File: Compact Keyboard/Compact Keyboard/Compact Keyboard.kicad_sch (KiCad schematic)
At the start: 3 parts, among them SW1 SW_Push

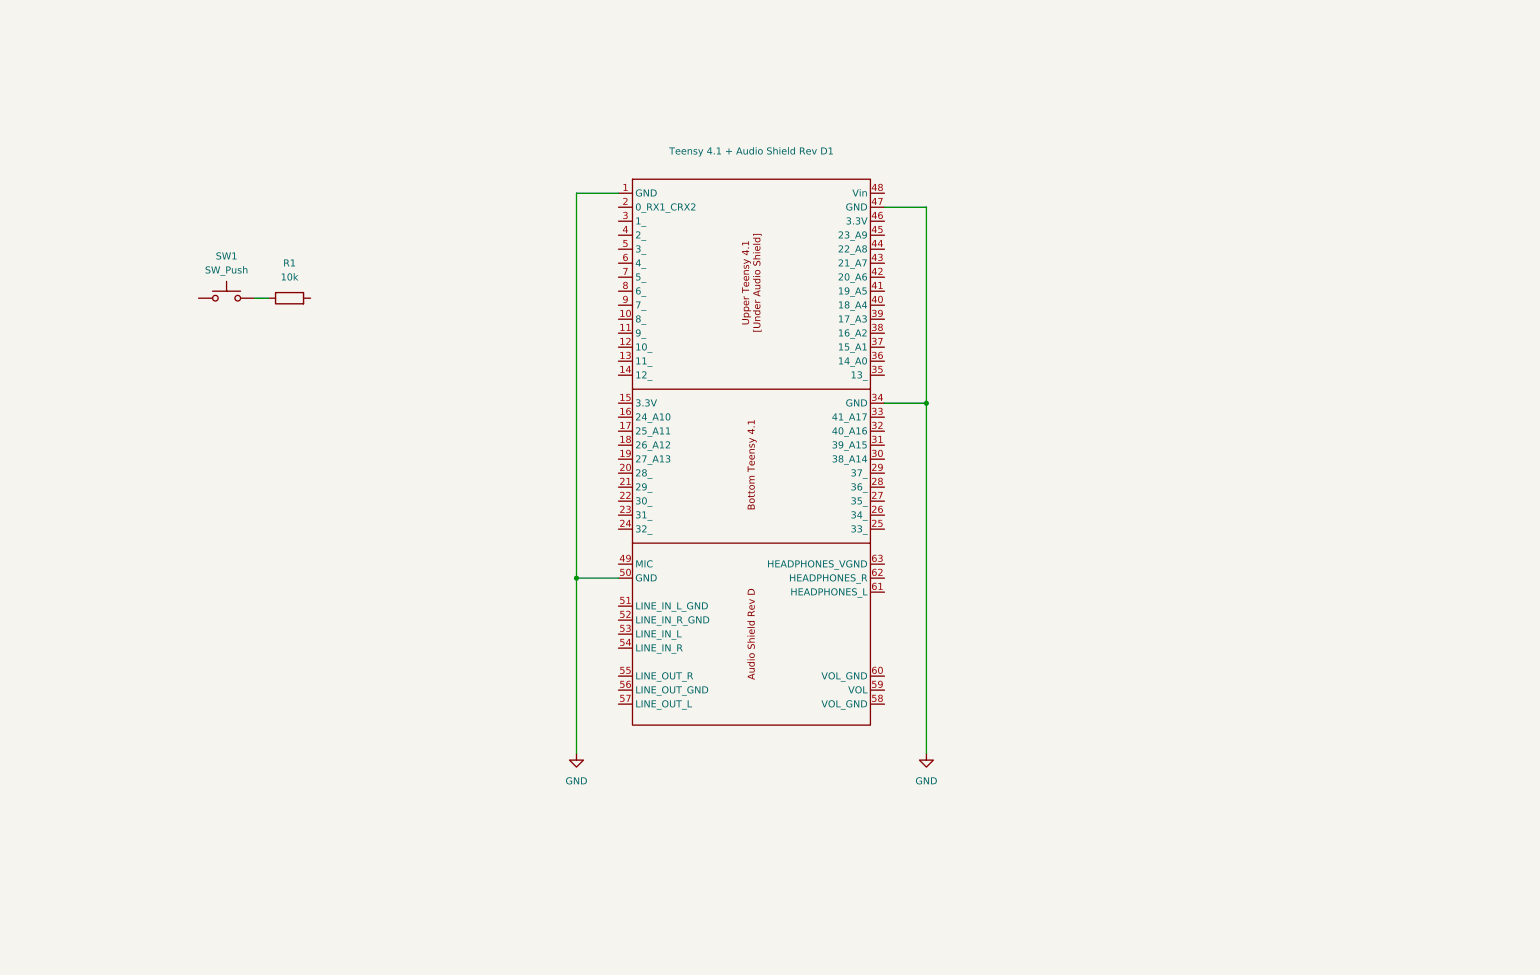
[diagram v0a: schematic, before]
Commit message: Smaller MUX, Main Board design
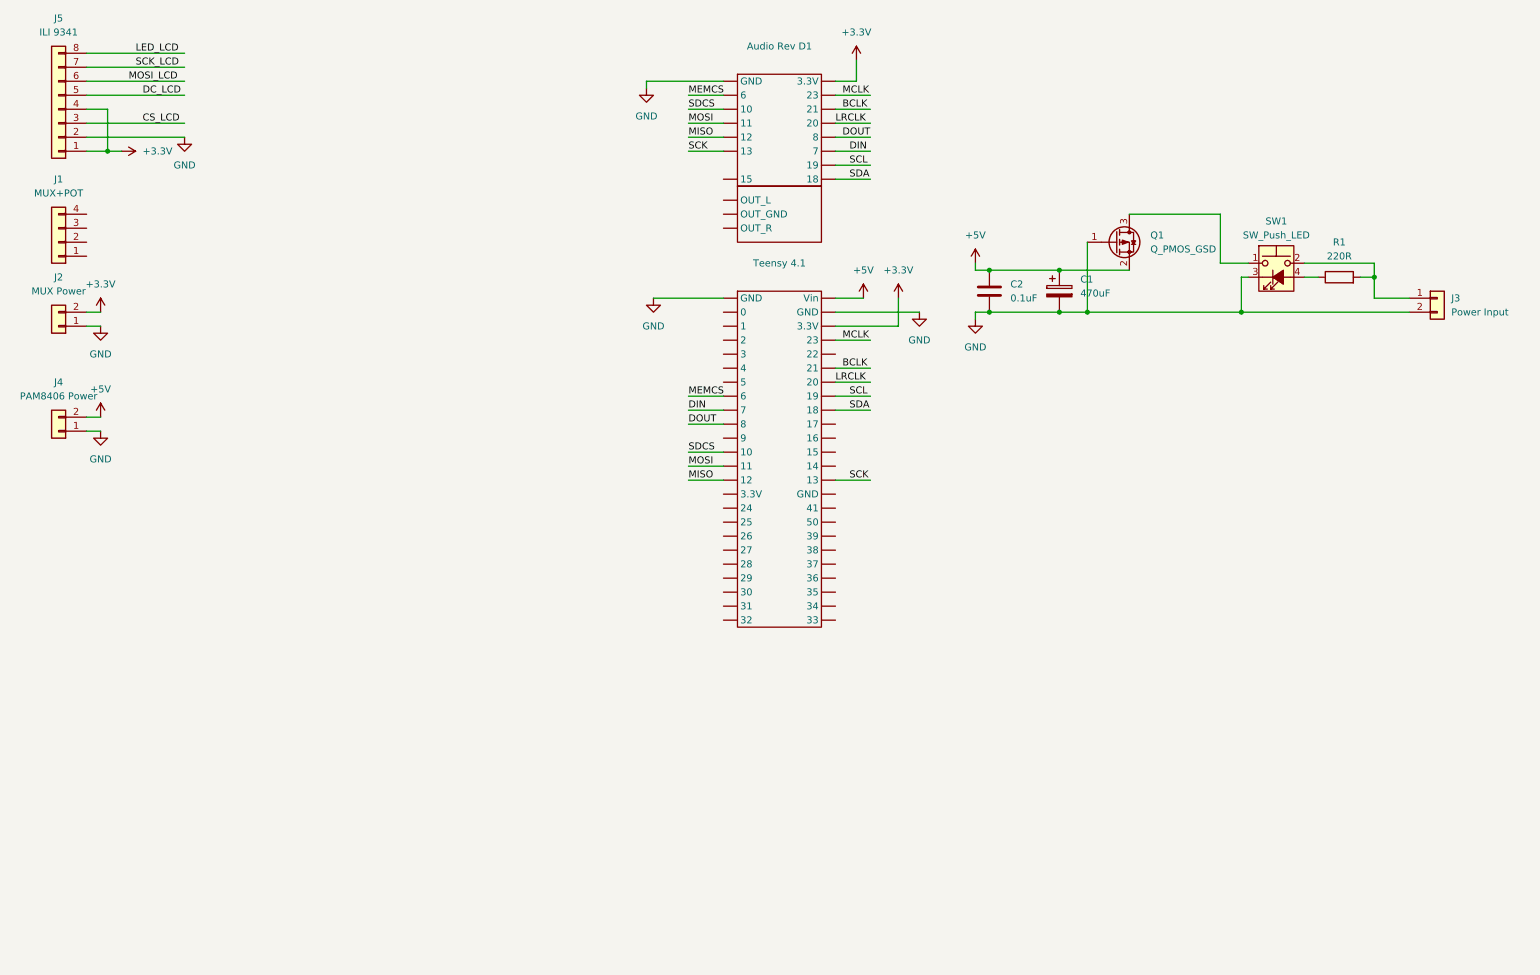
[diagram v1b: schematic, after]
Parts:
- removed SW1: SW_Push, symbol Switch:SW_Push
- removed Teensy 4.1 + Audio Shield Rev D1: ~, symbol Teensy:Teensy 4.1 + Audio Shield Rev D
- added Audio Rev D1: ~, symbol Teensy:Audio_Shield_Rev_D
- added C1: 470uF, symbol Device:C_Polarized
- added C2: 0.1uF, symbol Device:C
- added J1: MUX+POT, symbol Connector_Generic:Conn_01x04
- added J2: MUX Power, symbol Connector_Generic:Conn_01x02
- added J3: Power Input, symbol Connector_Generic:Conn_01x02
- added J4: PAM8406 Power, symbol Connector_Generic:Conn_01x02
- added J5: ILI 9341, symbol Connector_Generic:Conn_01x08
- added Q1: Q_PMOS_GSD, symbol Transistor_FET:Q_PMOS_GSD
- added SW1: SW_Push_LED, symbol Switch:SW_Push_LED
- added Teensy 4.1: ~, symbol Teensy:Teensy_4.1
- R1: value 10k -> 220R
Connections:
- net GND: now also Audio Rev D1. (18), C1.2, C2.2, J2.1 (Pin_1), J3.2 (Pin_2), J4.1 (Pin_1), J5.2 (Pin_2), Q1.1 (G), SW1.3 (K), Teensy 4.1. (33)
- net at R1.1: now also SW1.4 (A)
- net at R1.2: now also J3.1 (Pin_1), SW1.2
- new net: Q1.3 (D), SW1.1
- new net +3.3V: Audio Rev D1. (18), J2.2 (Pin_2), J5.1 (Pin_1), J5.4 (Pin_4), Teensy 4.1. (33)
- new net +5V: C1.1, C2.1, J4.2 (Pin_2), Q1.2 (S), Teensy 4.1. (33)
- new net BCLK: Audio Rev D1. (18), Teensy 4.1. (33)
- new net CS_LCD: J5.3 (Pin_3)
- new net DC_LCD: J5.5 (Pin_5)
- new net DIN: Audio Rev D1. (18), Teensy 4.1. (33)
- new net DOUT: Audio Rev D1. (18), Teensy 4.1. (33)
- new net LED_LCD: J5.8 (Pin_8)
- new net LRCLK: Audio Rev D1. (18), Teensy 4.1. (33)
- new net MCLK: Audio Rev D1. (18), Teensy 4.1. (33)
- new net MEMCS: Audio Rev D1. (18), Teensy 4.1. (33)
- new net MISO: Audio Rev D1. (18), Teensy 4.1. (33)
- new net MOSI: Audio Rev D1. (18), Teensy 4.1. (33)
- new net MOSI_LCD: J5.6 (Pin_6)
- new net SCK: Audio Rev D1. (18), Teensy 4.1. (33)
- new net SCK_LCD: J5.7 (Pin_7)
- new net SCL: Audio Rev D1. (18), Teensy 4.1. (33)
- new net SDA: Audio Rev D1. (18), Teensy 4.1. (33)
- new net SDCS: Audio Rev D1. (18), Teensy 4.1. (33)

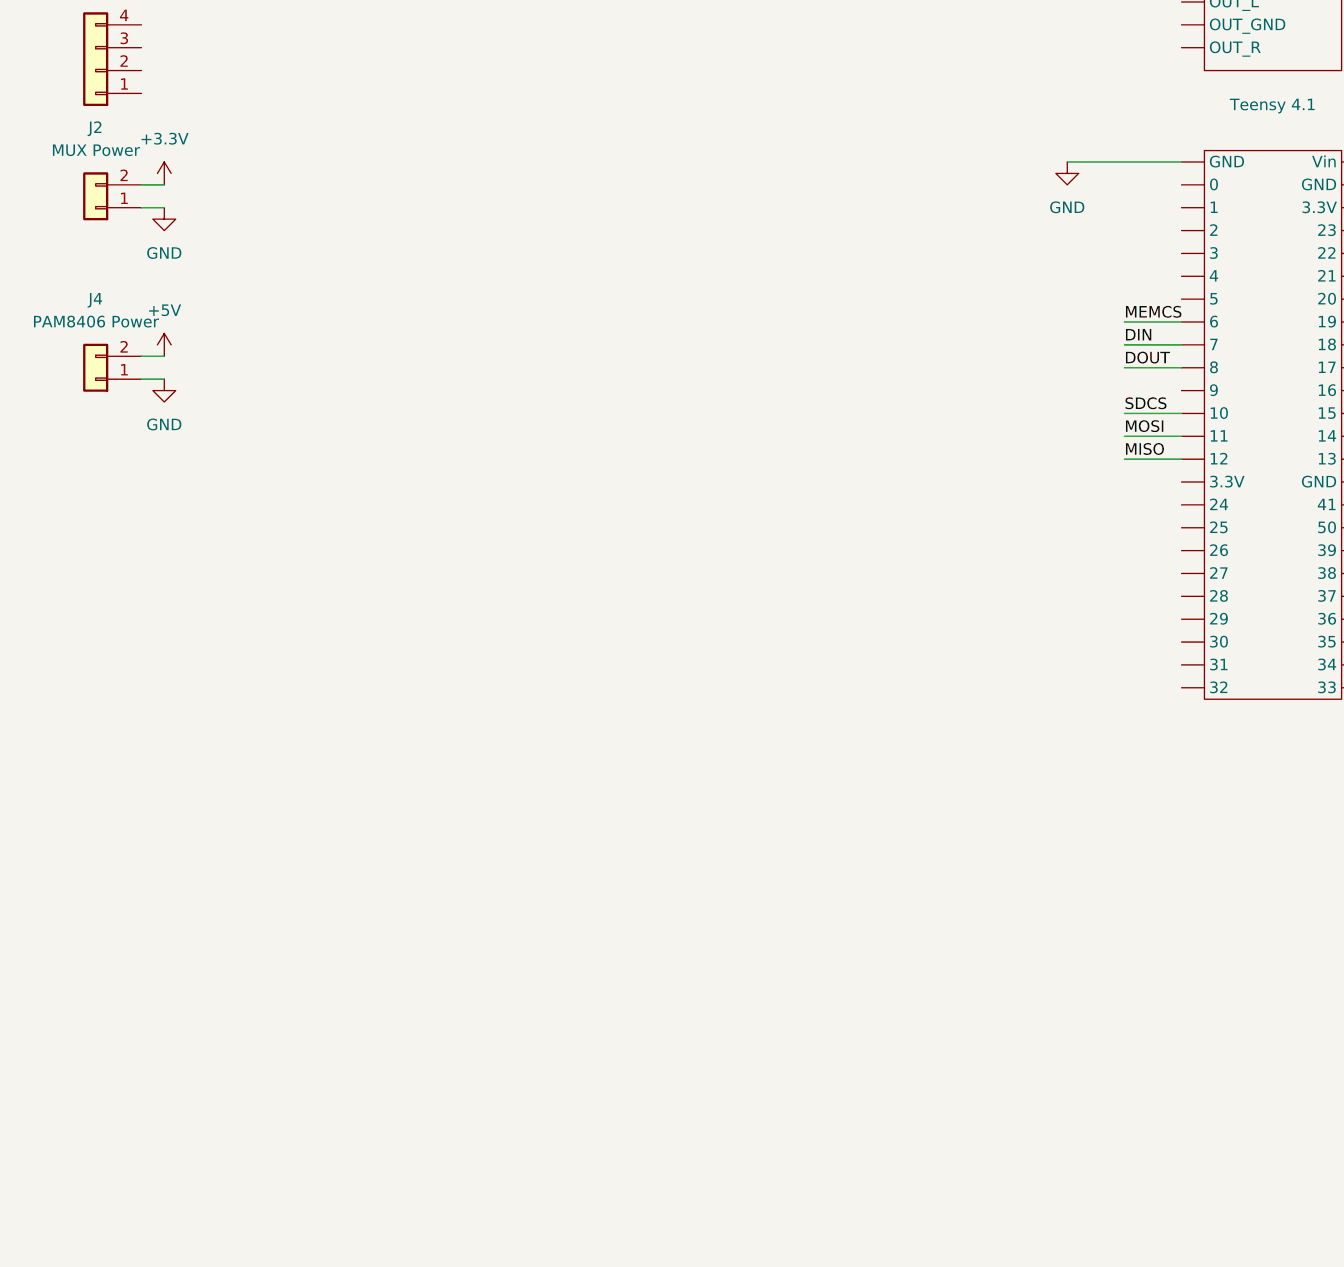
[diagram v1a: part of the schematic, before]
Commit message: More Inputs for Teensy
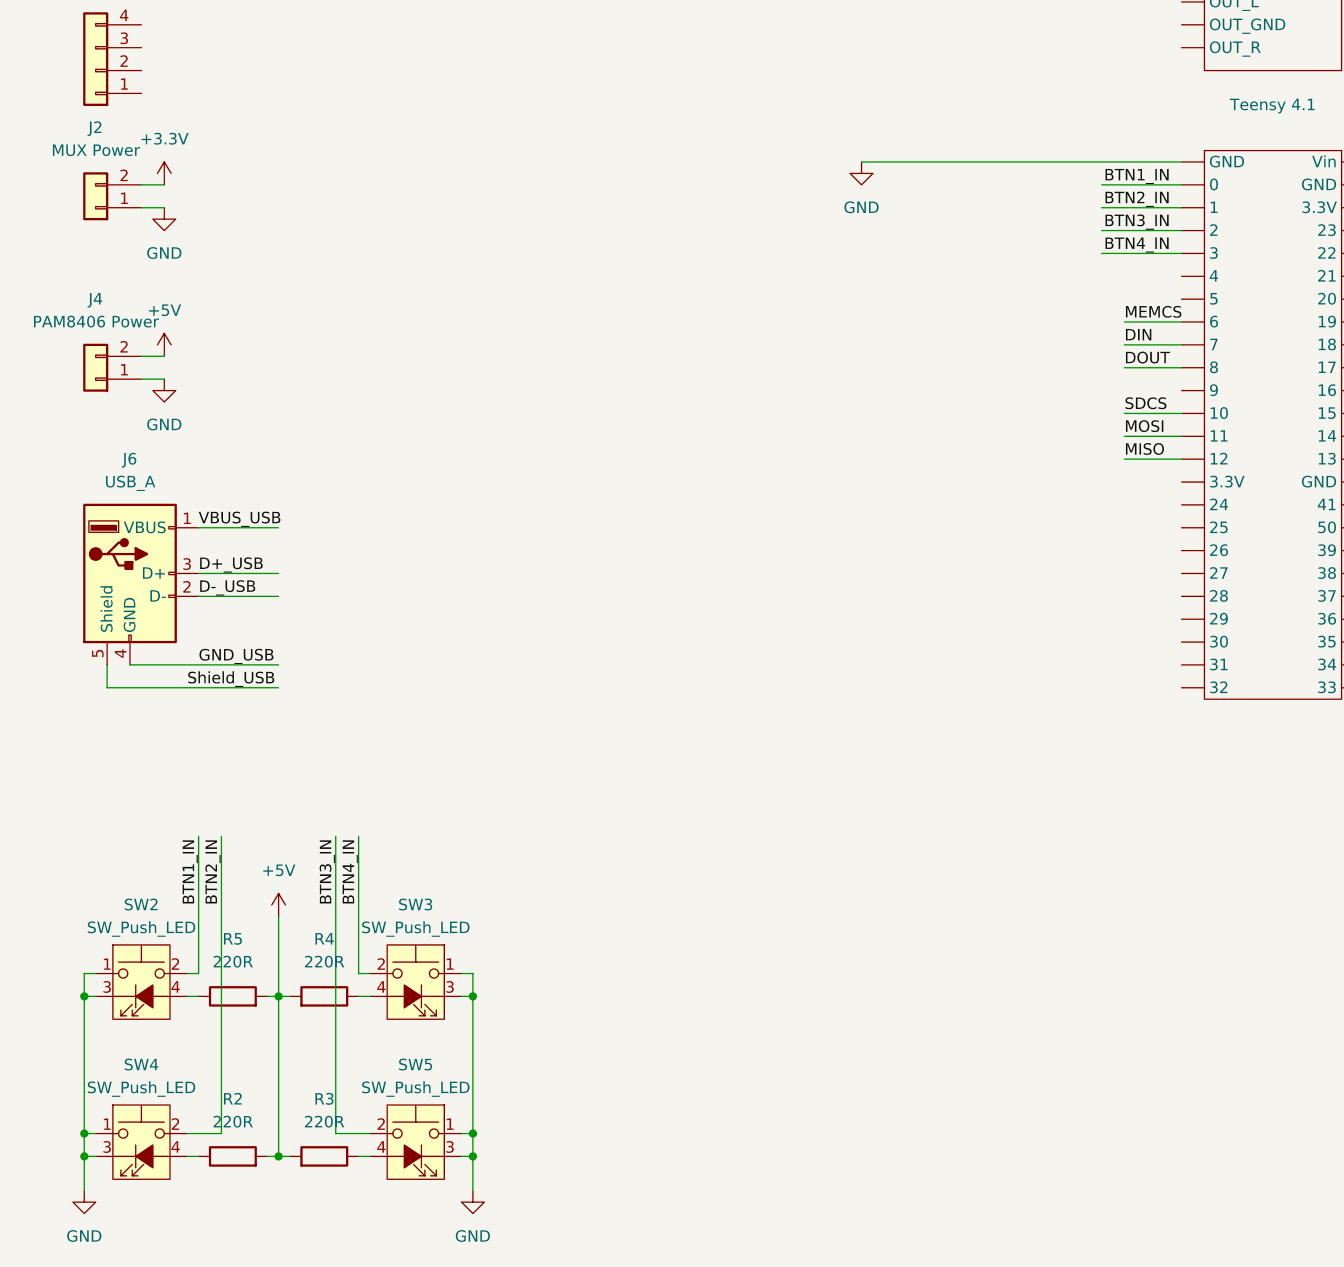
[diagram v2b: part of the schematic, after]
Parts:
- added J6: USB_A, symbol Connector:USB_A
- added R2, R3, R4, R5: 220R, symbol Device:R
- added SW2, SW3, SW4, SW5: SW_Push_LED, symbol Switch:SW_Push_LED
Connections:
- net +5V: now also R2.2, R3.2, R4.2, R5.2
- net GND: now also SW2.1, SW2.3 (K), SW3.1, SW3.3 (K), SW4.1, SW4.3 (K), SW5.1, SW5.3 (K)
- new net: R5.1, SW2.4 (A)
- new net: R2.1, SW4.4 (A)
- new net: R4.1, SW3.4 (A)
- new net: R3.1, SW5.4 (A)
- new net BTN1_IN: SW2.2, Teensy 4.1. (33)
- new net BTN2_IN: SW4.2, Teensy 4.1. (33)
- new net BTN3_IN: SW5.2, Teensy 4.1. (33)
- new net BTN4_IN: SW3.2, Teensy 4.1. (33)
- new net D+_USB: J6.3 (D+)
- new net D-_USB: J6.2 (D-)
- new net GND_USB: J6.4 (GND)
- new net Shield_USB: J6.5 (Shield)
- new net VBUS_USB: J6.1 (VBUS)
